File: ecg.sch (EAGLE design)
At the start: 1 part

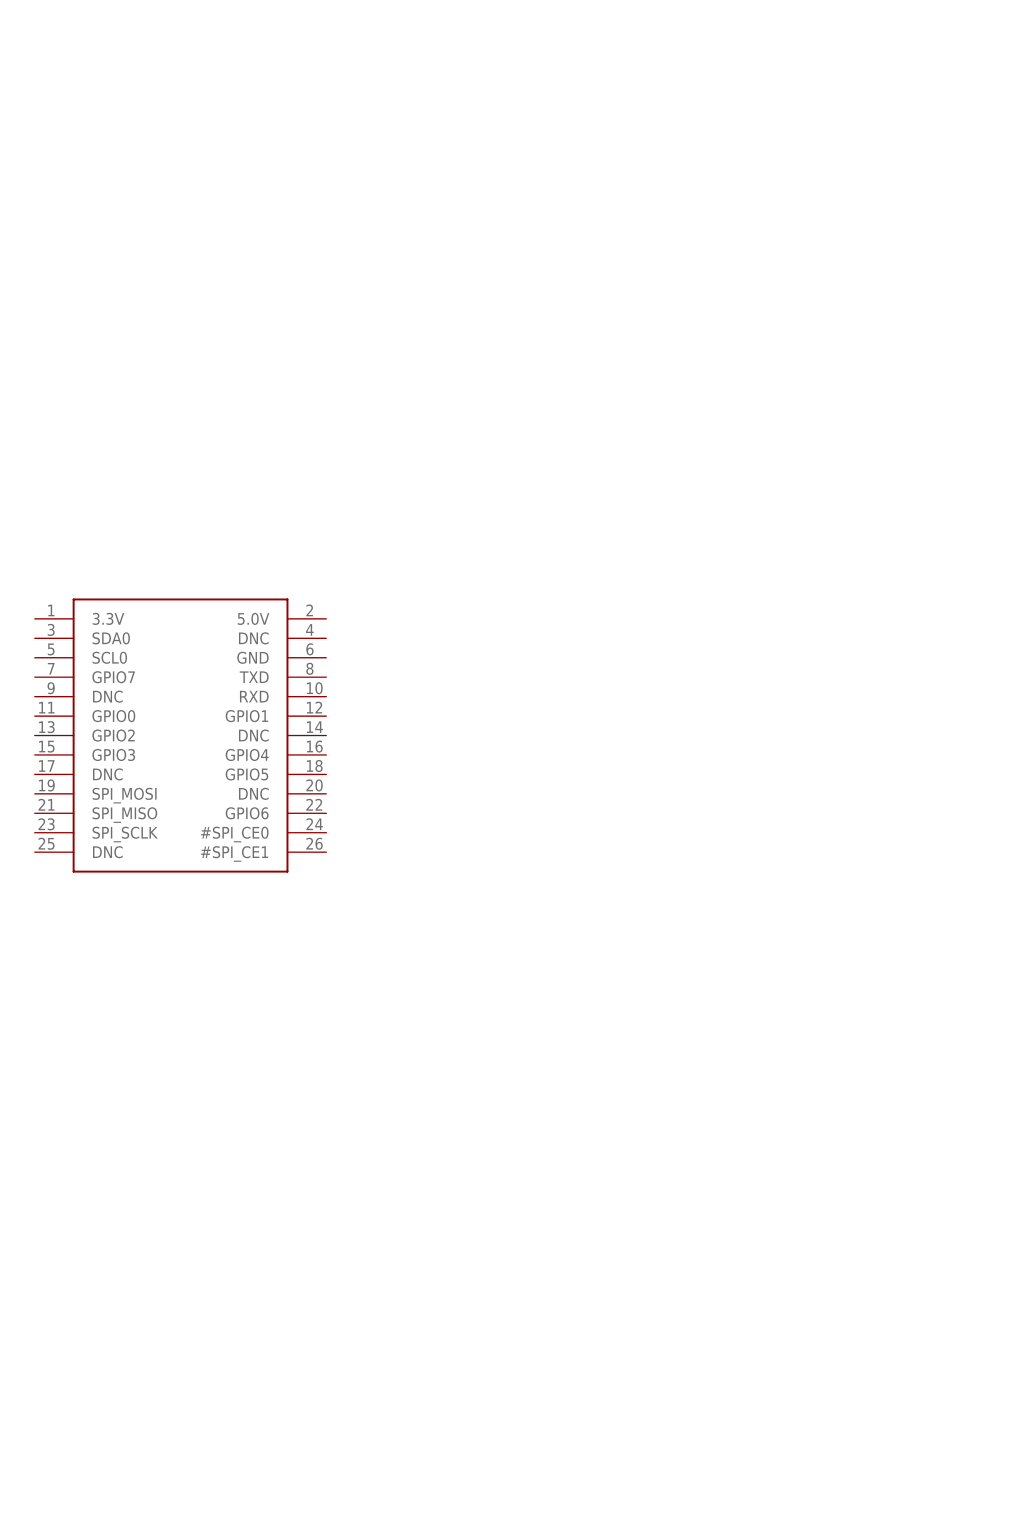
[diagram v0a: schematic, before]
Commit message: Added TMP102 and ADAS1000 to schematics
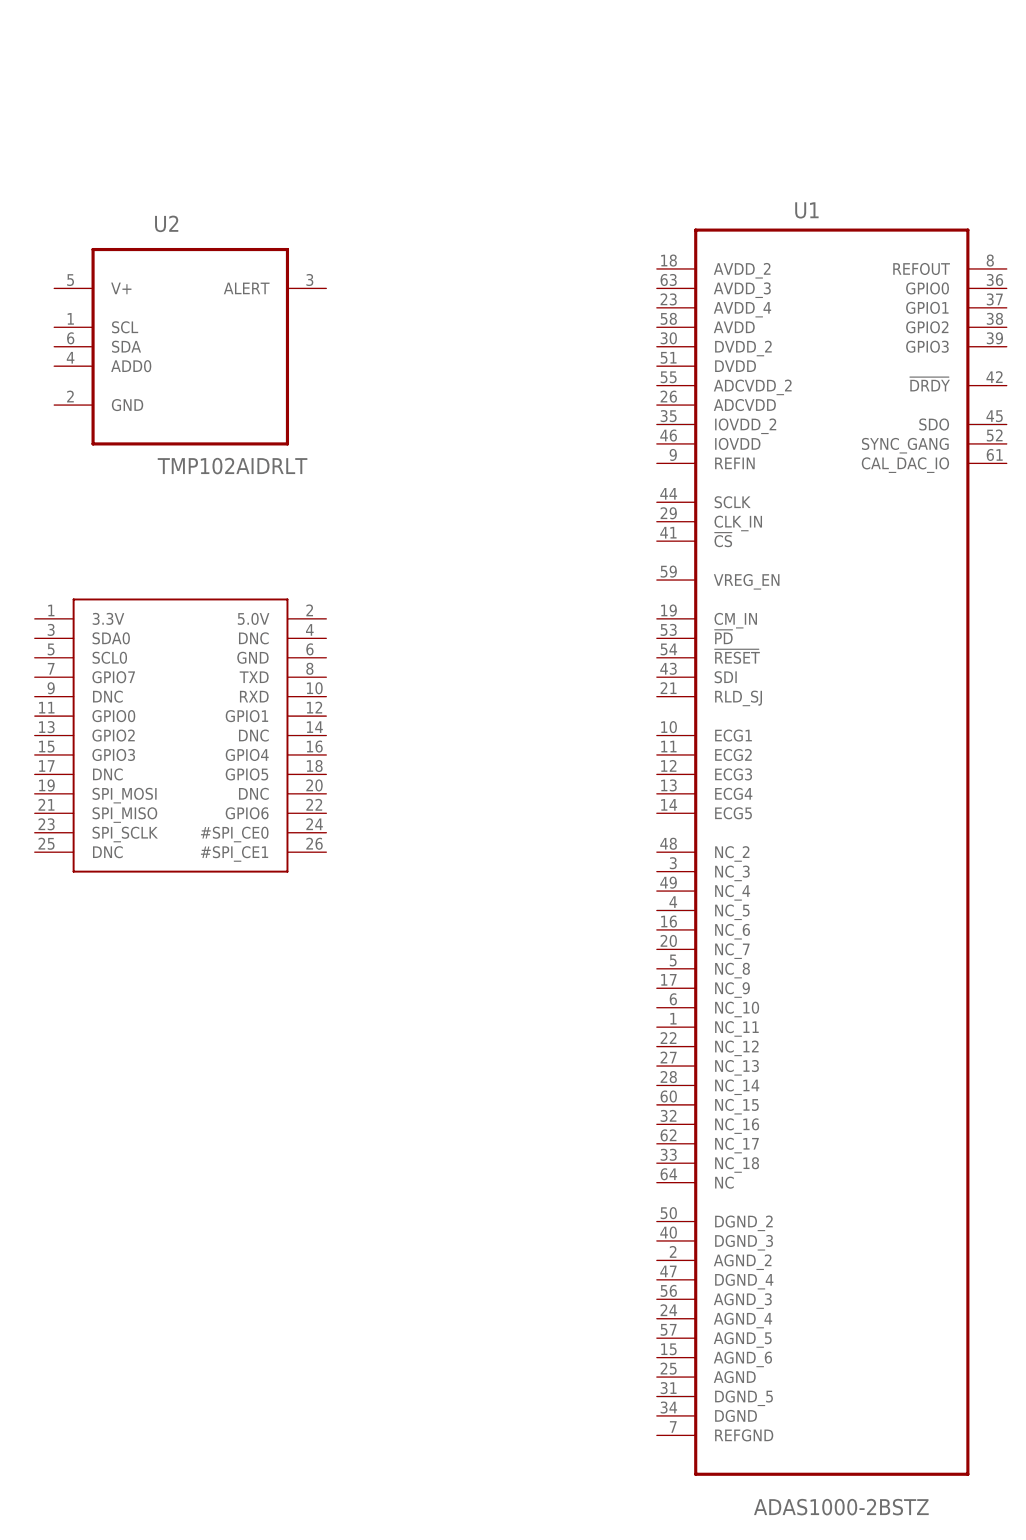
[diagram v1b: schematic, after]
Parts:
- added U1: ADAS1000-2BSTZ, ADAS1000:ADAS1000-2BSTZ
- added U2: TMP102AIDRLT, TMP102:TMP102AIDRLT
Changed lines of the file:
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@@
 <parts>
 <part name="U$1" library="microbuilder" deviceset="RASPBERRYPI_B" device="B"/>
+<part name="U1" library="ADAS1000" deviceset="ADAS1000-2BSTZ" device=""/>
+<part name="U2" library="TMP102" deviceset="TMP102AIDRLT" device=""/>
 </parts>
 <sheets>
@@
 <instances>
 <instance part="U$1" gate="G$1" x="71.12" y="48.26"/>
+<instance part="U1" gate="A" x="157.48" y="35.56"/>
+<instance part="U2" gate="A" x="73.66" y="101.6"/>
 </instances>
 <busses>

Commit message: Replaced ADAS1000-2 (which is a slave device and cannot be used in standalone application) with ADAS1000BSTZ which is a master device
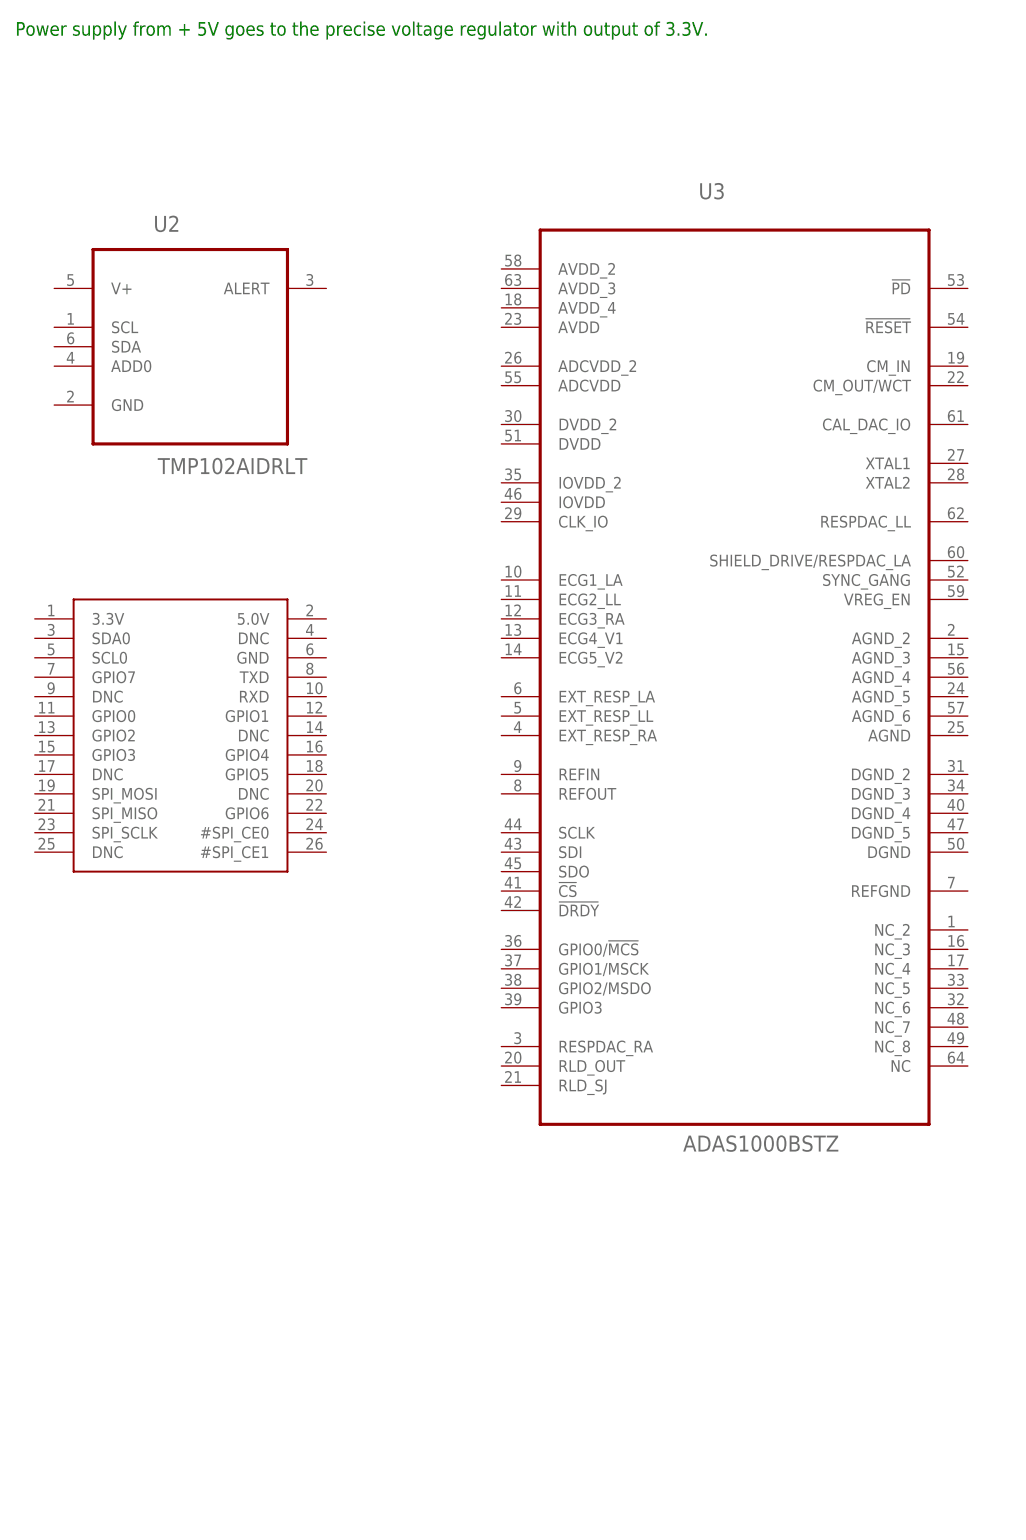
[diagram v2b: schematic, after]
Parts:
- removed U1: ADAS1000-2BSTZ, ADAS1000:ADAS1000-2BSTZ
- added U3: ADAS1000BSTZ, ADAS1000BSTZ:ADAS1000BSTZ
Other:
- note added: "Power supply from + 5V goes to the precise voltage regulator with output of 3.3V."
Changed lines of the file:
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@@
 <parts>
 <part name="U$1" library="microbuilder" deviceset="RASPBERRYPI_B" device="B"/>
-<part name="U1" library="ADAS1000" deviceset="ADAS1000-2BSTZ" device=""/>
 <part name="U2" library="TMP102" deviceset="TMP102AIDRLT" device=""/>
+<part name="U3" library="ADAS1000BSTZ" deviceset="ADAS1000BSTZ" device=""/>
 </parts>
 <sheets>
 <sheet>
 <plain>
+<text x="50.8" y="139.7" size="1.778" layer="91">Power supply from + 5V goes to the precise voltage regulator with output of 3.3V. </text>
 </plain>
 <instances>
 <instance part="U$1" gate="G$1" x="71.12" y="48.26"/>
-<instance part="U1" gate="A" x="157.48" y="35.56"/>
 <instance part="U2" gate="A" x="73.66" y="101.6"/>
+<instance part="U3" gate="A" x="144.78" y="58.42"/>
 </instances>
 <busses>
